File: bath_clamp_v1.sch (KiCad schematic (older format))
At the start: 18 parts, among them U10 LP2951-3.3_SOIC, U6 24AA025-OT, U7 LM337L_SO8, U9 MCP1804x-3302xOT

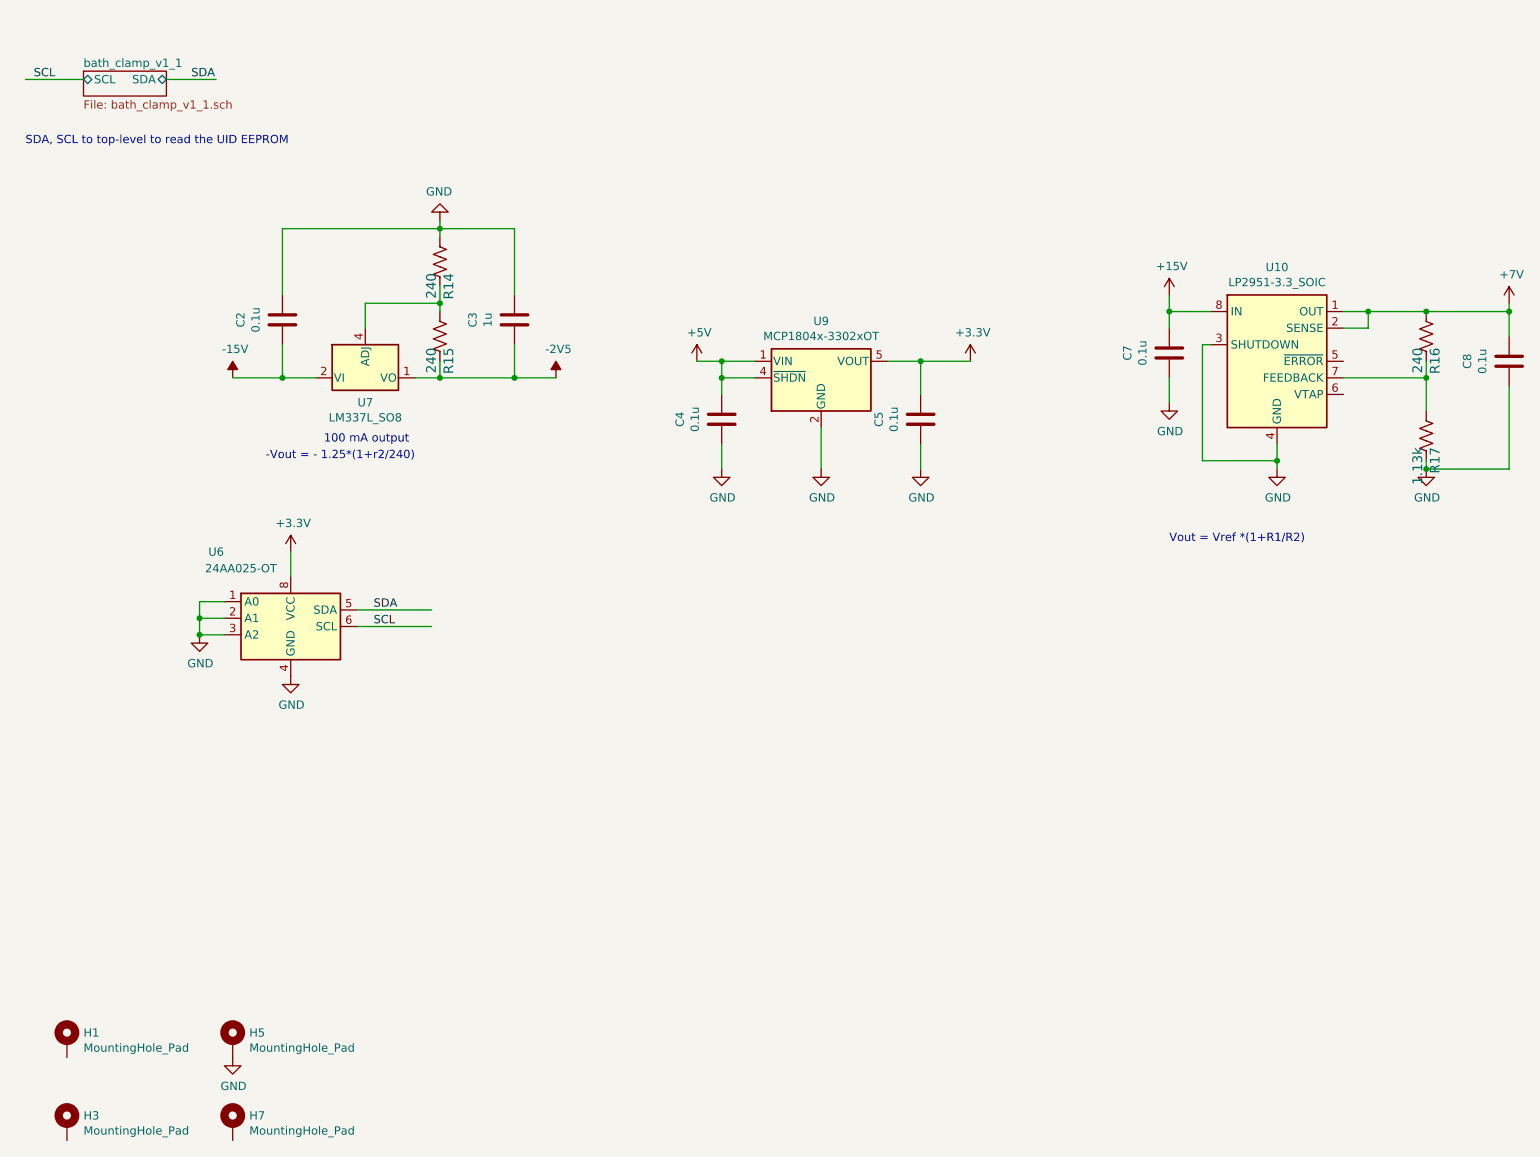
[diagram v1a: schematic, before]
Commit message: reduced ERC to just 4 warnings
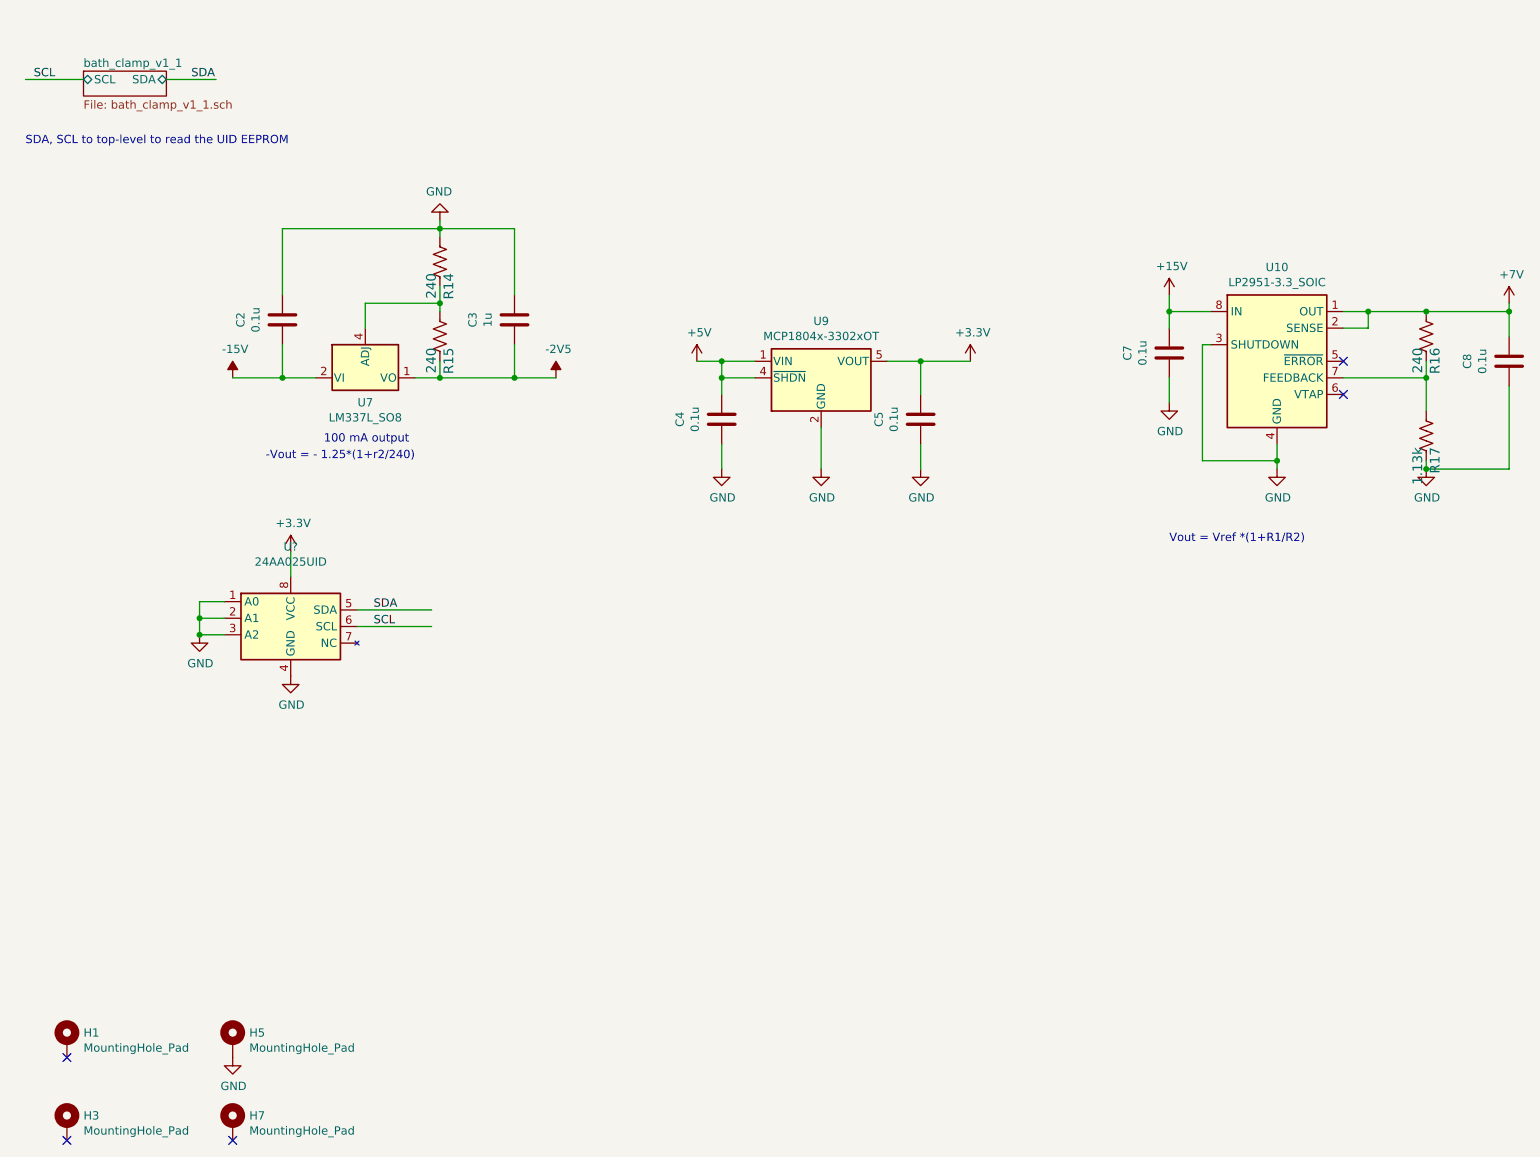
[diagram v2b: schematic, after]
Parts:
- removed U6: 24AA025-OT, Package_SO:SOIC-8_3.9x4.9mm_P1.27mm, symbol covg-kicad:24AA025-OT
- added U?: 24AA025UID, Package_SO:SOIC-8_3.9x4.9mm_P1.27mm, symbol covg-kicad:24AA025UID
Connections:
- no-connect marks 0 -> 5
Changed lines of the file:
@@
-$EndComp
-$Comp
-L covg-kicad:24AA025-OT U6
-U 1 1 60ECBA53
-P 2250 4350
-F 0 "U6" H 1800 4800 50  0000 C CNN
-F 1 "24AA025-OT" H 1950 4700 50  0000 C CNN
-F 2 "Package_SO:SOIC-8_3.9x4.9mm_P1.27mm" H 2250 4350 50  0001 C CNN
-F 3 "https://ww1.microchip.com/downloads/en/DeviceDoc/20005202A.pdf" H 2250 4350 50  0001 C CNN
-F 4 "24AA025UIDT-I/SN" H 2250 4931 50  0001 C CNN "Manf#"
-	1    2250 4350
-	1    0    0    -1
 $EndComp
 $Comp
@@
 Text Notes 650  1450 0    50   ~ 0
 SDA, SCL to top-level to read the UID EEPROM
-Text Label 2750 4250 0    50   ~ 0
-SDA
 Text Label 2750 4350 0    50   ~ 0
 SCL
@@
 Wire Wire Line
 	8750 2450 9100 2450
-Wire Wire Line
-	2650 4250 3100 4250
 Wire Wire Line
 	2650 4350 3100 4350
@@
 Wire Wire Line
 	2250 3900 2250 4050
+NoConn ~ 8600 2750
+NoConn ~ 8600 2950
+NoConn ~ 900  6950
+NoConn ~ 900  7450
+NoConn ~ 1900 7450
+Wire Wire Line
+	2650 4250 3100 4250
+Text Label 2750 4250 0    50   ~ 0
+SDA
+$Comp
+L covg-kicad:24AA025UID U?
+U 1 1 627267F8
+P 2250 4350
+F 0 "U?" H 2250 4831 50  0000 C CNN
+F 1 "24AA025UID" H 2250 4740 50  0000 C CNN
+F 2 "Package_SO:SOIC-8_3.9x4.9mm_P1.27mm" H 2250 4350 50  0001 C CNN
+F 3 "https://ww1.microchip.com/downloads/en/DeviceDoc/20005202A.pdf" H 2250 4350 50  0001 C CNN
+	1    2250 4350
+	1    0    0    -1
+$EndComp
 $EndSCHEMATC

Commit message: updates to pcb layout
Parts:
- added R51: DNI, Resistor_SMD:R_0603_1608Metric, symbol Device:R_US
- H1, H3, H5, H7: footprint (none) -> MountingHole:MountingHole_3.2mm_M3_DIN965_Pad
- gave numbers to parts that had none: 1
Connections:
- wire segments 61 -> 62
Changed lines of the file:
@@
 F 0 "H1" H 1000 6899 50  0000 L CNN
 F 1 "MountingHole_Pad" H 1000 6808 50  0000 L CNN
-F 2 "" H 900 6850 50  0001 C CNN
+F 2 "MountingHole:MountingHole_3.2mm_M3_DIN965_Pad" H 900 6850 50  0001 C CNN
 F 3 "~" H 900 6850 50  0001 C CNN
 	1    900  6850
@@
 F 0 "H3" H 1000 7399 50  0000 L CNN
 F 1 "MountingHole_Pad" H 1000 7308 50  0000 L CNN
-F 2 "" H 900 7350 50  0001 C CNN
+F 2 "MountingHole:MountingHole_3.2mm_M3_DIN965_Pad" H 900 7350 50  0001 C CNN
 F 3 "~" H 900 7350 50  0001 C CNN
 	1    900  7350
@@
 F 0 "H7" H 2000 7399 50  0000 L CNN
 F 1 "MountingHole_Pad" H 2000 7308 50  0000 L CNN
-F 2 "" H 1900 7350 50  0001 C CNN
+F 2 "MountingHole:MountingHole_3.2mm_M3_DIN965_Pad" H 1900 7350 50  0001 C CNN
 F 3 "~" H 1900 7350 50  0001 C CNN
 	1    1900 7350
@@
 F 0 "H5" H 2000 6899 50  0000 L CNN
 F 1 "MountingHole_Pad" H 2000 6808 50  0000 L CNN
-F 2 "" H 1900 6850 50  0001 C CNN
+F 2 "MountingHole:MountingHole_3.2mm_M3_DIN965_Pad" H 1900 6850 50  0001 C CNN
 F 3 "~" H 1900 6850 50  0001 C CNN
 	1    1900 6850
@@
 SDA
 $Comp
-L covg-kicad:24AA025UID U?
+L covg-kicad:24AA025UID U6
 U 1 1 627267F8
 P 2250 4350
-F 0 "U?" H 2250 4831 50  0000 C CNN
+F 0 "U6" H 2250 4831 50  0000 C CNN
 F 1 "24AA025UID" H 2250 4740 50  0000 C CNN
 F 2 "Package_SO:SOIC-8_3.9x4.9mm_P1.27mm" H 2250 4350 50  0001 C CNN
@@
 	1    0    0    -1
 $EndComp
+$Comp
+L Device:R_US R?
+U 1 1 6277A90A
+P 1050 7100
+AR Path="/6032F251/6277A90A" Ref="R?"  Part="1"
+AR Path="/6277A90A" Ref="R51"  Part="1"
+F 0 "R51" V 997 7168 59  0000 L CNN
+F 1 "DNI" V 1102 7168 59  0000 L CNN
+F 2 "Resistor_SMD:R_0603_1608Metric" H 1050 7100 50  0001 C CNN
+F 3 "" H 1050 7100 50  0001 C CNN
+F 4 "RC0603FR-07240RL" H 997 7268 50  0001 C CNN "Manf#"
+F 5 "1%" H 1050 7100 50  0001 C CNN "Tolerance"
+	1    1050 7100
+	0    -1   -1   0
+$EndComp
+$Comp
+L power:GND #PWR0136
+U 1 1 6277B1AB
+P 1200 7100
+F 0 "#PWR0136" H 1200 6850 50  0001 C CNN
+F 1 "GND" H 1205 6927 50  0000 C CNN
+F 2 "" H 1200 7100 50  0001 C CNN
+F 3 "" H 1200 7100 50  0001 C CNN
+	1    1200 7100
+	0    -1   -1   0
+$EndComp
+Wire Wire Line
+	900  7100 900  6950
 $EndSCHEMATC

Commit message: made sheet for Howland
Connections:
- no-connect marks 5 -> 4
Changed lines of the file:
@@
 $Descr A4 11693 8268
 encoding utf-8
-Sheet 1 6
+Sheet 1 7
 Title "Bath/Guard Clamp"
 Date "2021-04-06"
@@
 NoConn ~ 8600 2750
 NoConn ~ 8600 2950
-NoConn ~ 900  6950
 NoConn ~ 900  7450
 NoConn ~ 1900 7450
@@
 U 1 1 627267F8
 P 2250 4350
-F 0 "U6" H 2250 4831 50  0000 C CNN
+F 0 "U6" H 2050 4850 50  0000 C CNN
 F 1 "24AA025UID" H 2250 4740 50  0000 C CNN
 F 2 "Package_SO:SOIC-8_3.9x4.9mm_P1.27mm" H 2250 4350 50  0001 C CNN
@@
 $EndComp
 Wire Wire Line
-	900  7100 900  6950
+	900  6950 900  7100
 $EndSCHEMATC

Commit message: layout updates; part positioning
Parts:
- added R71: 0, Resistor_SMD:R_0603_1608Metric, symbol Device:R_US
- R51: Manf# RC0603FR-07240RL -> (none)
- U6: Manf# (none) -> 24AA025UIDT-I/SN
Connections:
- wire segments 62 -> 65
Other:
- moved on the sheet: R17
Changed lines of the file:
@@
 L Device:R_US R?
 U 1 1 60E4F39D
-P 9100 3200
+P 9100 3050
 AR Path="/6032F251/60E4F39D" Ref="R?"  Part="1"
 AR Path="/60E4F39D" Ref="R17"  Part="1"
-F 0 "R17" V 9047 3268 59  0000 L CNN
-F 1 "1.13k" V 9152 3268 59  0000 L CNN
-F 2 "Resistor_SMD:R_0603_1608Metric" H 9100 3200 50  0001 C CNN
-F 3 "" H 9100 3200 50  0001 C CNN
-F 4 "RC0603FR-071K13L" H 9047 3368 50  0001 C CNN "Manf#"
-F 5 "1%" H 9100 3200 50  0001 C CNN "Tolerance"
-	1    9100 3200
+F 0 "R17" V 9047 3118 59  0000 L CNN
+F 1 "1.13k" V 9152 3118 59  0000 L CNN
+F 2 "Resistor_SMD:R_0603_1608Metric" H 9100 3050 50  0001 C CNN
+F 3 "" H 9100 3050 50  0001 C CNN
+F 4 "RC0603FR-071K13L" H 9047 3218 50  0001 C CNN "Manf#"
+F 5 "1%" H 9100 3050 50  0001 C CNN "Tolerance"
+	1    9100 3050
 	-1   0    0    1
 $EndComp
@@
 F 3 "" H 1700 4400 50  0001 C CNN
 	1    1700 4400
-	1    0    0    -1
-$EndComp
-$Comp
-L power:GND #PWR0107
-U 1 1 60FD35B5
-P 1900 6950
-F 0 "#PWR0107" H 1900 6700 50  0001 C CNN
-F 1 "GND" H 1905 6777 50  0000 C CNN
-F 2 "" H 1900 6950 50  0001 C CNN
-F 3 "" H 1900 6950 50  0001 C CNN
-	1    1900 6950
 	1    0    0    -1
 $EndComp
@@
 	9100 2750 9100 2850
 Wire Wire Line
-	9100 3400 9100 3350
+	9100 3400 9100 3200
 Wire Wire Line
 	8600 2850 9100 2850
 Wire Wire Line
-	9100 2850 9100 3050
+	9100 2850 9100 2900
 Wire Wire Line
 	8200 3400 8200 3350
@@
 F 2 "Package_SO:SOIC-8_3.9x4.9mm_P1.27mm" H 2250 4350 50  0001 C CNN
 F 3 "https://ww1.microchip.com/downloads/en/DeviceDoc/20005202A.pdf" H 2250 4350 50  0001 C CNN
+F 4 "24AA025UIDT-I/SN" H 2250 4350 50  0001 C CNN "Manf#"
 	1    2250 4350
 	1    0    0    -1
@@
 F 2 "Resistor_SMD:R_0603_1608Metric" H 1050 7100 50  0001 C CNN
 F 3 "" H 1050 7100 50  0001 C CNN
-F 4 "RC0603FR-07240RL" H 997 7268 50  0001 C CNN "Manf#"
+F 4 "" H 997 7268 50  0001 C CNN "Manf#"
 F 5 "1%" H 1050 7100 50  0001 C CNN "Tolerance"
 	1    1050 7100
@@
 Wire Wire Line
 	900  6950 900  7100
+$Comp
+L Device:R_US R?
+U 1 1 61765356
+P 2150 7100
+AR Path="/6032F251/61765356" Ref="R?"  Part="1"
+AR Path="/61765356" Ref="R71"  Part="1"
+F 0 "R71" V 2097 7168 59  0000 L CNN
+F 1 "0" V 2202 7168 59  0000 L CNN
+F 2 "Resistor_SMD:R_0603_1608Metric" H 2150 7100 50  0001 C CNN
+F 3 "" H 2150 7100 50  0001 C CNN
+F 4 "RC0603FR-070RL" H 2097 7268 50  0001 C CNN "Manf#"
+F 5 "1%" H 2150 7100 50  0001 C CNN "Tolerance"
+	1    2150 7100
+	0    -1   -1   0
+$EndComp
+Wire Wire Line
+	2000 7100 1900 7100
+Wire Wire Line
+	1900 7100 1900 6950
+$Comp
+L power:GND #PWR0107
+U 1 1 6176698C
+P 2350 7100
+F 0 "#PWR0107" H 2350 6850 50  0001 C CNN
+F 1 "GND" H 2355 6927 50  0000 C CNN
+F 2 "" H 2350 7100 50  0001 C CNN
+F 3 "" H 2350 7100 50  0001 C CNN
+	1    2350 7100
+	0    -1   -1   0
+$EndComp
+Wire Wire Line
+	2350 7100 2300 7100
 $EndSCHEMATC

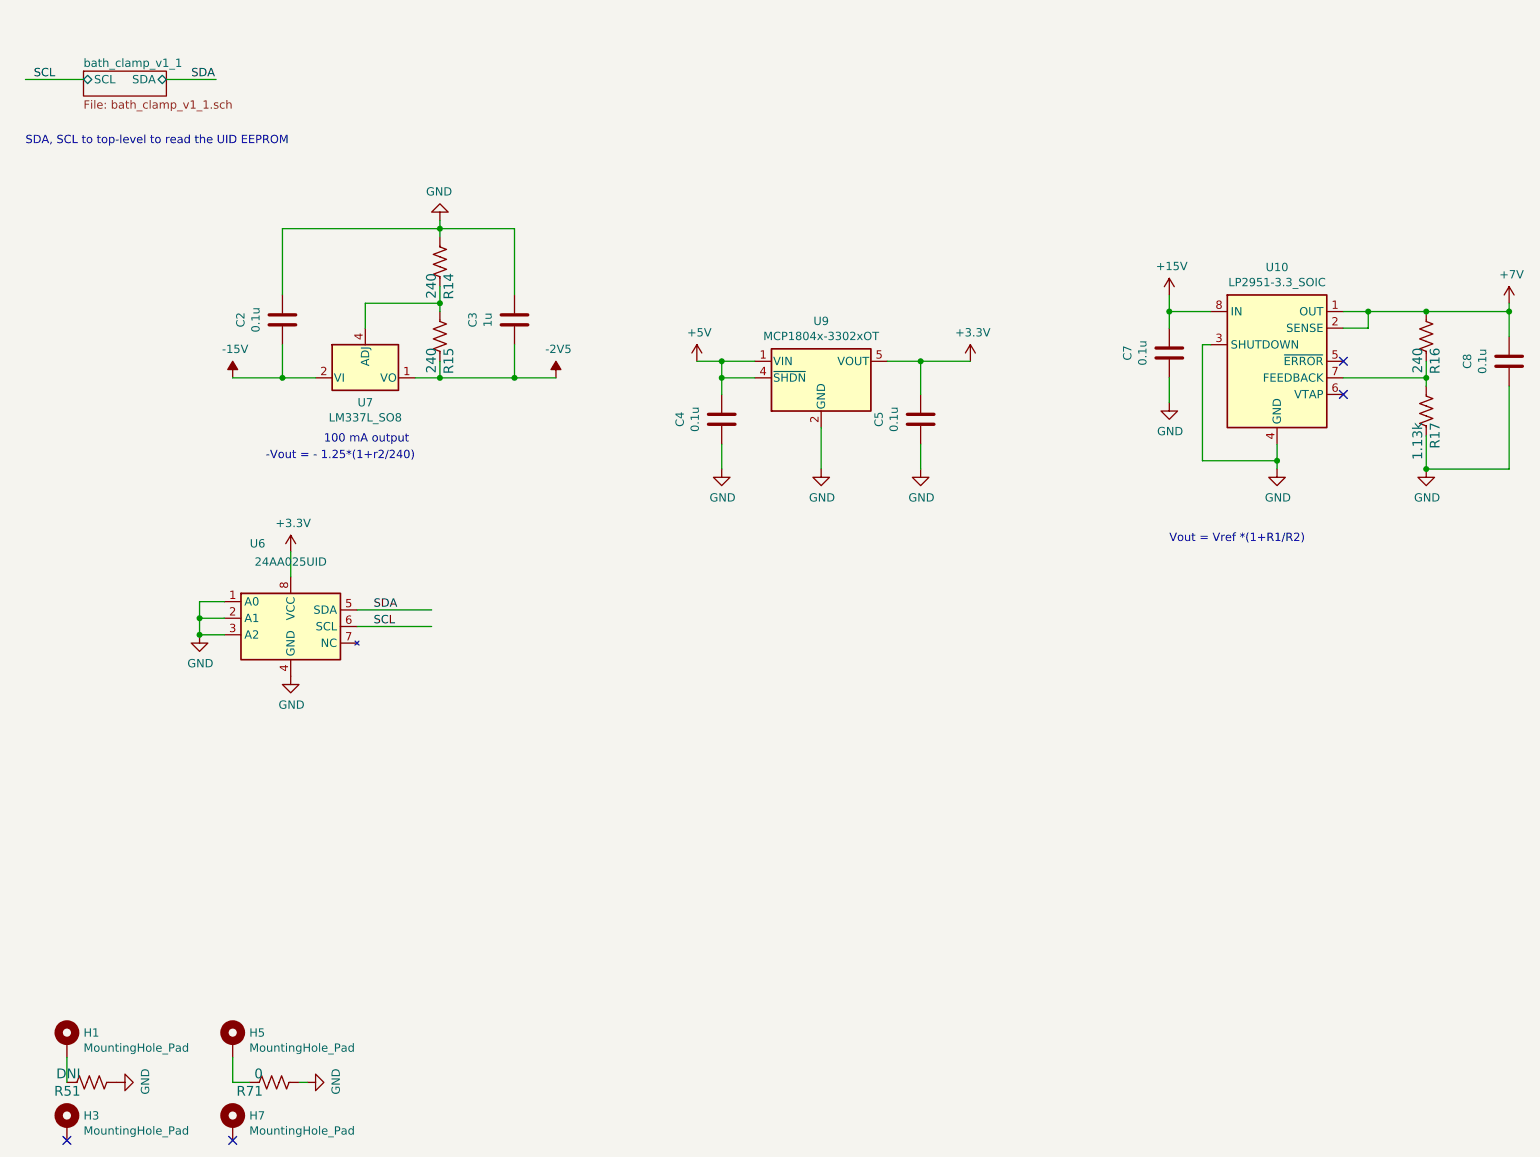
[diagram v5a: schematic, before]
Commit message: updates to README
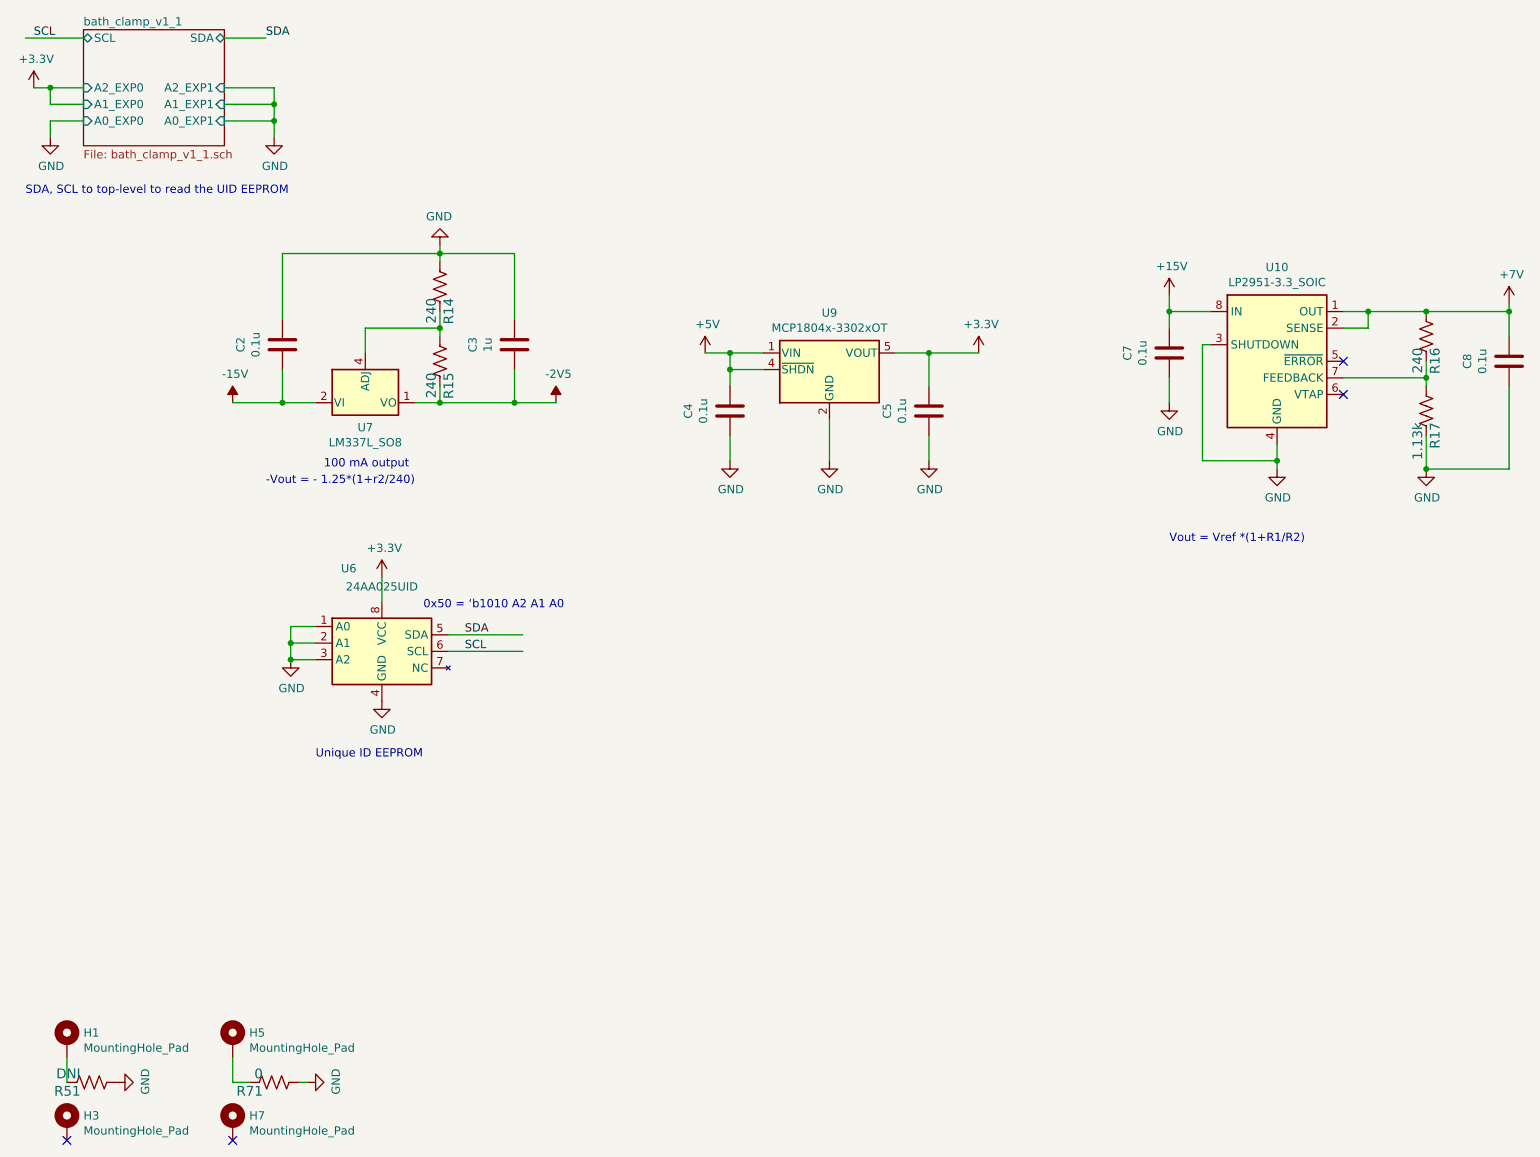
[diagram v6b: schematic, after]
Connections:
- wire segments 65 -> 77
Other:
- note added: "0x50 = ‘b1010 A2 A1 A0"
- note added: "Unique ID EEPROM"
- moved on the sheet: C2, C3, C4, C5, R14, R15, U6, U7, U9
